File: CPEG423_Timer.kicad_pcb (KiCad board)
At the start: 2 copper layers, 101.6 x 101.6 mm, 78 parts, among them SW1 SW_PUSH, SW2 SW_PUSH, U1 3.0 V, U10 74HC04, U11 CD74HC30, U12 SN74HC132, U13 SN74HC163, U14 SN74HC163, U15 74HC04, U16 CD74HC30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

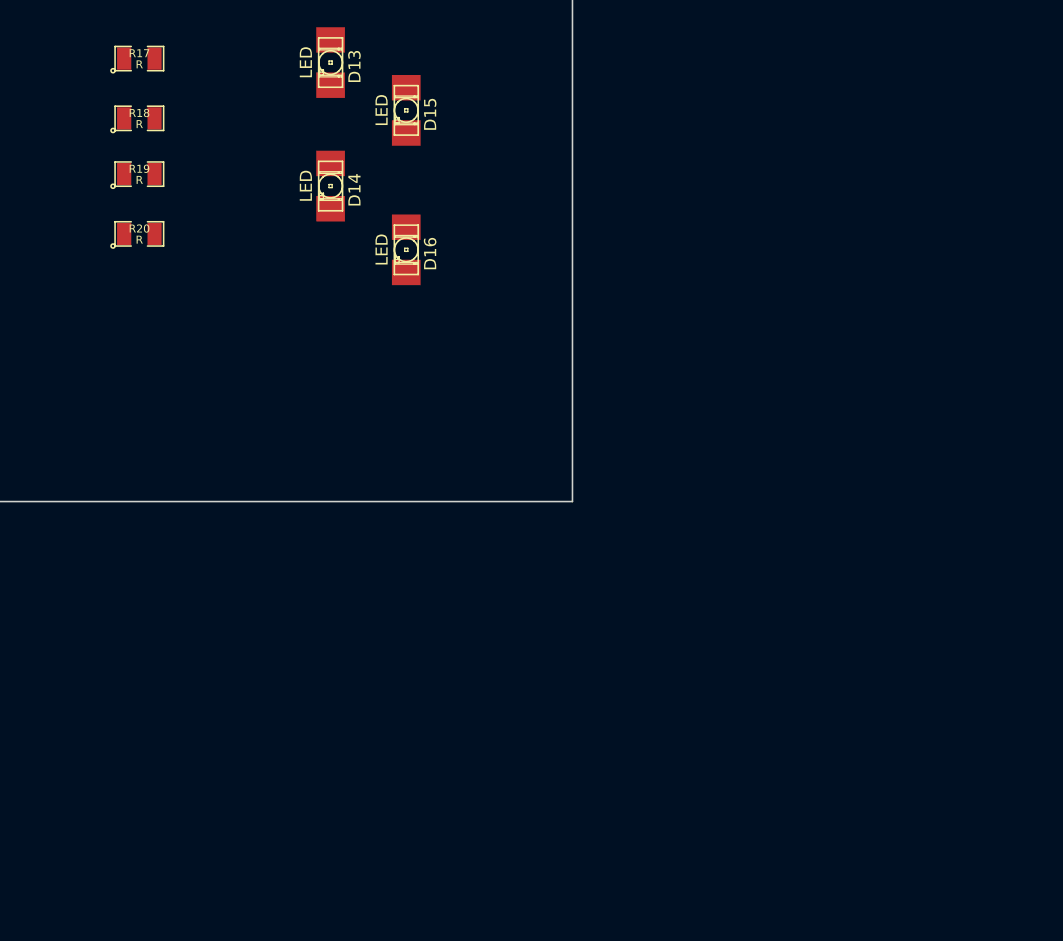
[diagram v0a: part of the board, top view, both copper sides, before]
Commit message: Completed Netlist & Updated Layout
Associated OSC with Si501 footprint (.cmp).  Reread netlist into layout
editor (.kicad_pcb) adding battery and oscillator footprints.
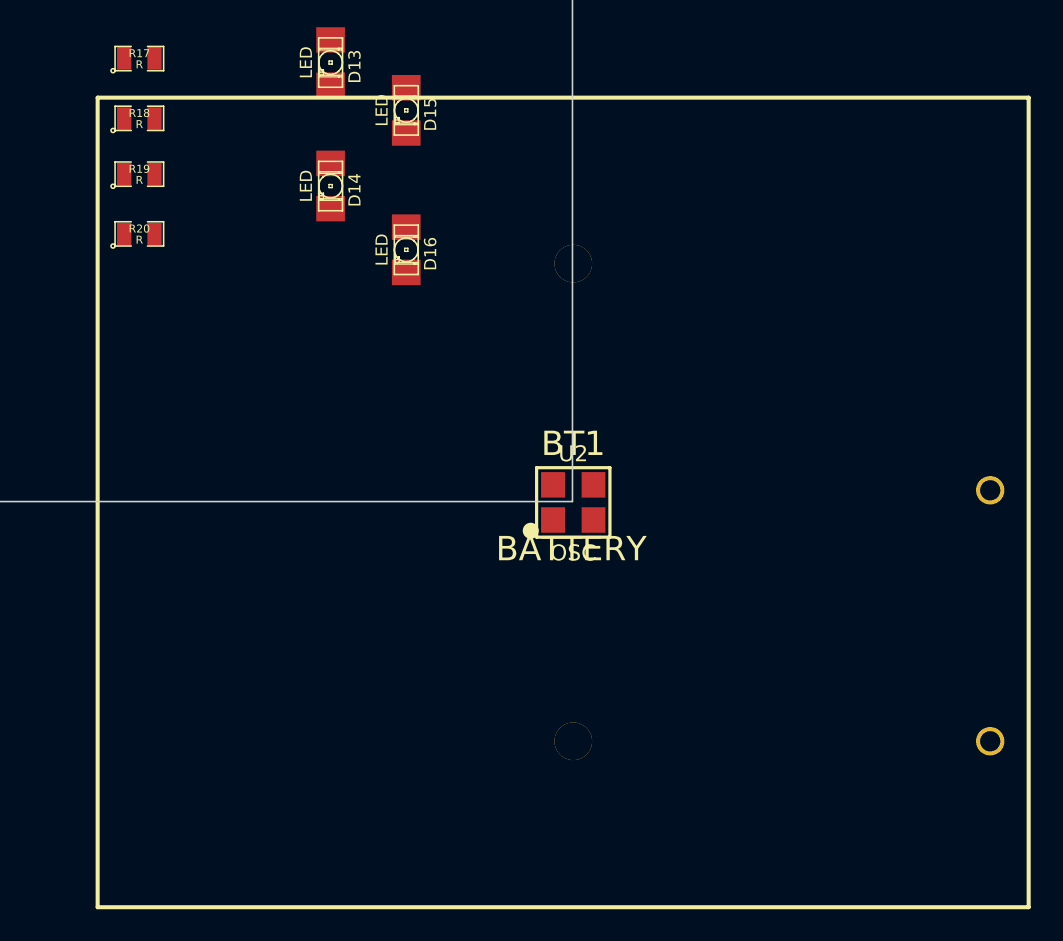
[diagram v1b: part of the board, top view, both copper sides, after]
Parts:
- added BT1: BATTERY, BC3AAPC, F.Cu at (186.0, 209.4)
- added U2: OSC, Si501, F.Cu at (186.0, 209.4)
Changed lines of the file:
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@@
-(kicad_pcb (version 3) (host pcbnew "(2013-may-18)-stable")
+(kicad_pcb (version 3) (host pcbnew "(2013-07-07 BZR 4022)-stable")
   (general
-    (links 244)
-    (no_connects 244)
-    (area -8.218531 107.645999 185.978001 210.35645)
+    (links 249)
+    (no_connects 249)
+    (area 84.277999 107.645999 185.978001 209.346001)
     (thickness 1.6)
     (drawings 4)
     (tracks 0)
     (zones 0)
-    (modules 78)
+    (modules 80)
     (nets 69)
   )
@@
     (pad_to_mask_clearance 0)
     (aux_axis_origin 0 0)
-    (visible_elements 7FFFFFFF)
+    (visible_elements 7FFFFBFF)
     (pcbplotparams
       (layerselection 3178497)
@@
     )
   )
+  (module Si501 (layer F.Cu)
+    (at 185.978001 209.351001)
+    (fp_text reference U2 (at 0 -3.048) (layer F.SilkS)
+      (effects (font (size 1 1) (thickness 0.15)))
+    )
+    (fp_text value OSC (at 0 3.175) (layer F.SilkS)
+      (effects (font (size 1 1) (thickness 0.15)))
+    )
+    (fp_line (start -2.3 -2.18) (end 2.3 -2.18) (layer F.SilkS) (width 0.2))
+    (fp_line (start -2.3 -2.18) (end -2.3 2.18) (layer F.SilkS) (width 0.2))
+    (fp_line (start -2.3 2.18) (end 2.3 2.18) (layer F.SilkS) (width 0.2))
+    (fp_line (start 2.3 2.18) (end 2.3 -2.18) (layer F.SilkS) (width 0.2))
+    (fp_circle (center -2.667 1.778) (end -2.667 1.524) (layer F.SilkS) (width 0.5))
+    (fp_circle (center 0 0) (end 0 0) (layer F.SilkS) (width 0.5))
+    (pad 2 smd rect (at 1.27 1.1) (size 1.5 1.6)
+      (layers F.Cu F.Paste F.Mask)
+      (net 23 GND)
+    )
+    (pad 3 smd rect (at 1.27 -1.1) (size 1.5 1.6)
+      (layers F.Cu F.Paste F.Mask)
+      (net 6 /main_counter/Osc_In)
+    )
+    (pad 4 smd rect (at -1.27 -1.1) (size 1.5 1.6)
+      (layers F.Cu F.Paste F.Mask)
+      (net 68 VCC)
+    )
+    (pad 1 smd rect (at -1.27 1.1) (size 1.5 1.6)
+      (layers F.Cu F.Paste F.Mask)
+    )
+  )
+  (module BC3AAPC (layer F.Cu)
+    (at 185.978001 209.351001)
+    (fp_text reference BT1 (at 0 -3.683) (layer F.SilkS)
+      (effects (font (size 1.524 1.524) (thickness 0.254)))
+    )
+    (fp_text value BATTERY (at -0.127 2.921) (layer F.SilkS)
+      (effects (font (size 1.524 1.524) (thickness 0.254)))
+    )
+    (fp_line (start 28.575 25.4) (end 28.575 -25.4) (layer F.SilkS) (width 0.254))
+    (fp_line (start -29.845 -25.4) (end -29.845 25.4) (layer F.SilkS) (width 0.254))
+    (fp_line (start -29.845 -25.4) (end 28.575 -25.4) (layer F.SilkS) (width 0.254))
+    (fp_line (start -29.845 25.4) (end 28.575 25.4) (layer F.SilkS) (width 0.254))
+    (pad "" thru_hole circle (at 0 -14.986) (size 2.3622 2.3622) (drill 2.3622)
+      (layers *.Cu *.Mask F.SilkS)
+    )
+    (pad 1 thru_hole circle (at 26.162 14.986) (size 1.778 1.778) (drill 1.27)
+      (layers *.Cu *.Mask F.SilkS)
+      (net 28 N-0000015)
+    )
+    (pad "" thru_hole circle (at 0 14.986) (size 2.3622 2.3622) (drill 2.3622)
+      (layers *.Cu *.Mask F.SilkS)
+    )
+    (pad 2 thru_hole circle (at 26.162 -0.762) (size 1.778 1.778) (drill 1.27)
+      (layers *.Cu *.Mask F.SilkS)
+      (net 23 GND)
+    )
+  )
